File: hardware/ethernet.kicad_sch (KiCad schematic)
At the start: 31 parts, among them J2 HR871150C, U2 W5500, X2 25MHz

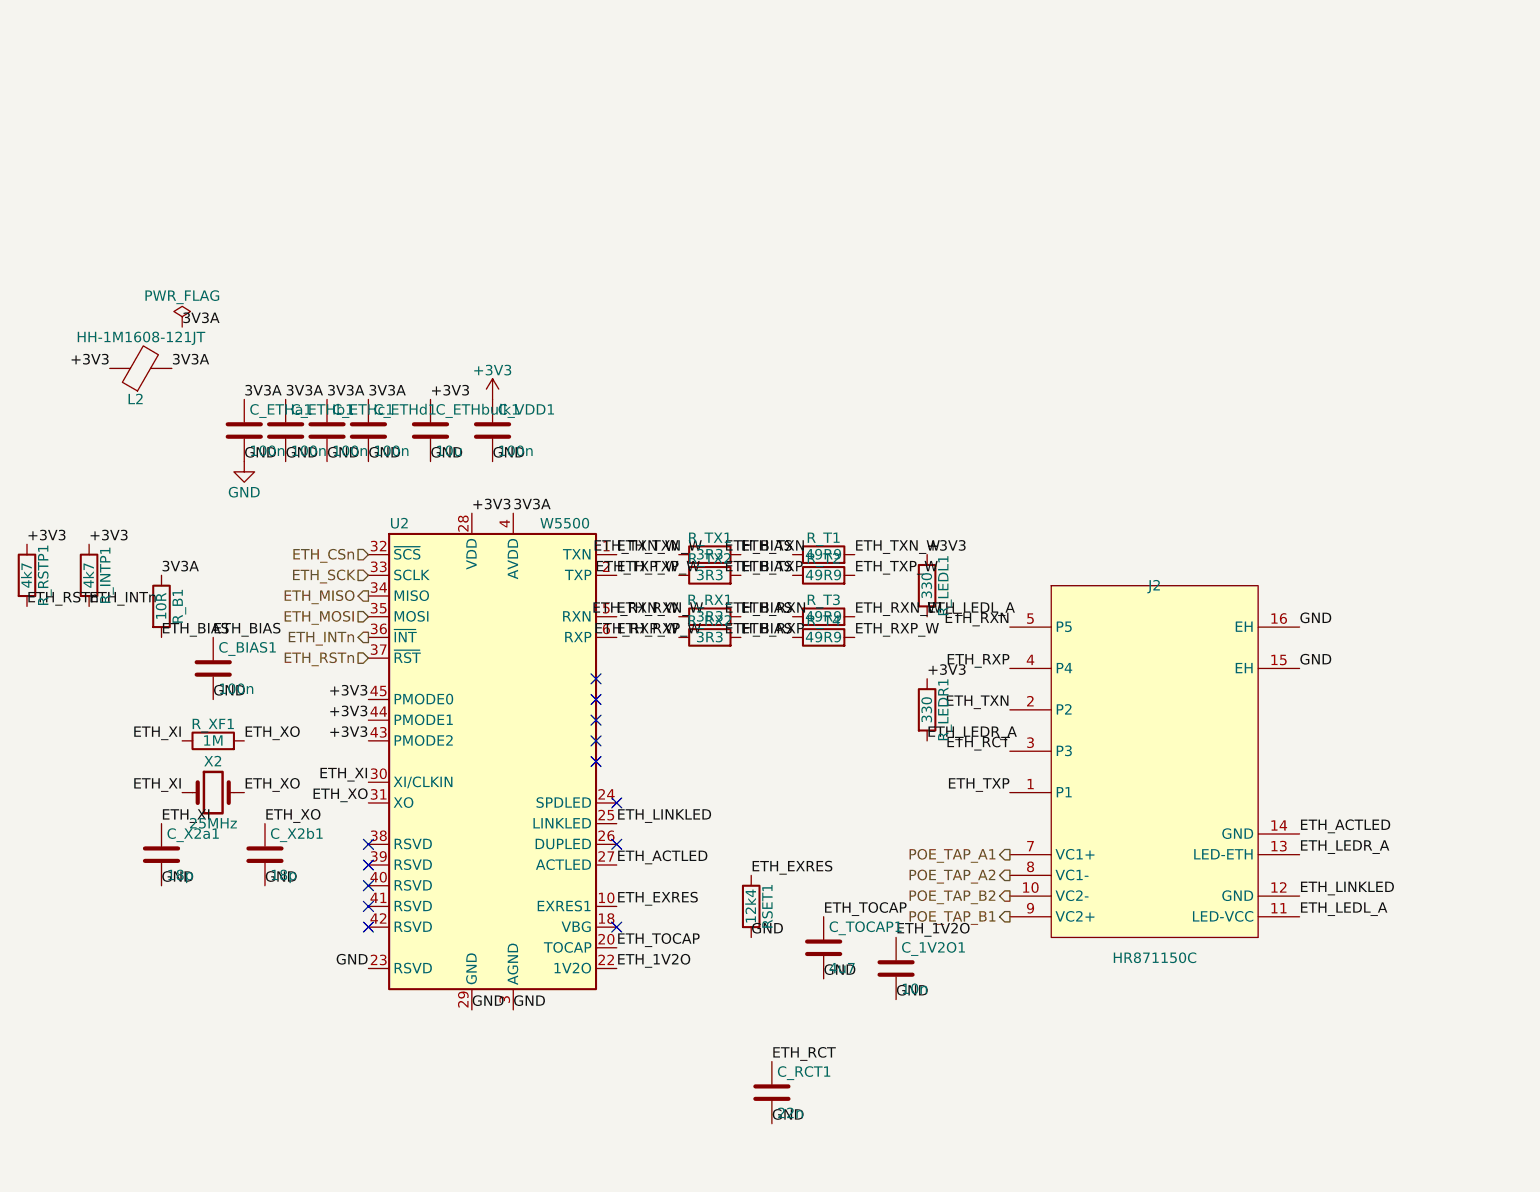
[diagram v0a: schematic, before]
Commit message: hardware: updated board design (reference renumbering, LED polarity fix, crystal symbol upgrade)
Replaces the schematics/PCB/project file with the latest design. Key
changes, verified before committing (netlist-check.py: 124 checks, 0
failures; ERC unchanged at 3 known pin_not_driven findings on W5500 SPI
inputs, same severity-policy artifact as before):

- Component reference designators changed from descriptive names
  (R_ATN, C_3V3, D_BR1, etc.) to plain auto-numbered ones (R15, C9, D1,
  etc.) -- intentional, since descriptive names were ending up on the
  silkscreen; they belong in the BOM instead. docs/netlist-spec.nets
  updated to match via a UUID-verified old-ref -> new-ref mapping (every
  renamed symbol's KiCad UUID was unchanged, confirming these are pure
  renames with no electrical difference), not a hand transcription.
- LED1's wiring was corrected: the old schematic had its anode tied to
  GND and cathode driven by LED_A (backwards -- confirmed via each net's
  pinfunction annotation in the exported netlist, K_1/A_2, which is
  fixed by the Device:LED symbol regardless of reference numbering).
  The new schematic has cathode-to-GND, anode-to-LED_A, the correct
  orientation.
- X1/X2 changed from Device:Crystal (2-pin) to Device:Crystal_GND24
  (4-pin, case-ground on pins 2/4) -- a more accurate symbol for the
  real SMD crystal package. netlist-spec.nets updated accordingly
  (XOUT/ETH_XO now reference pin 3, GND gained the four case pins).

mcu.kicad_sch was supplied separately (missing from the first archive);
confirmed it has no further sub-sheet references and all its symbols'
footprint names resolve against the existing hardware/lib/adapter.pretty/
library, which was deliberately left untouched along with fp-lib-table,
sym-lib-table, and .konnect/ -- none of those changed in this update.
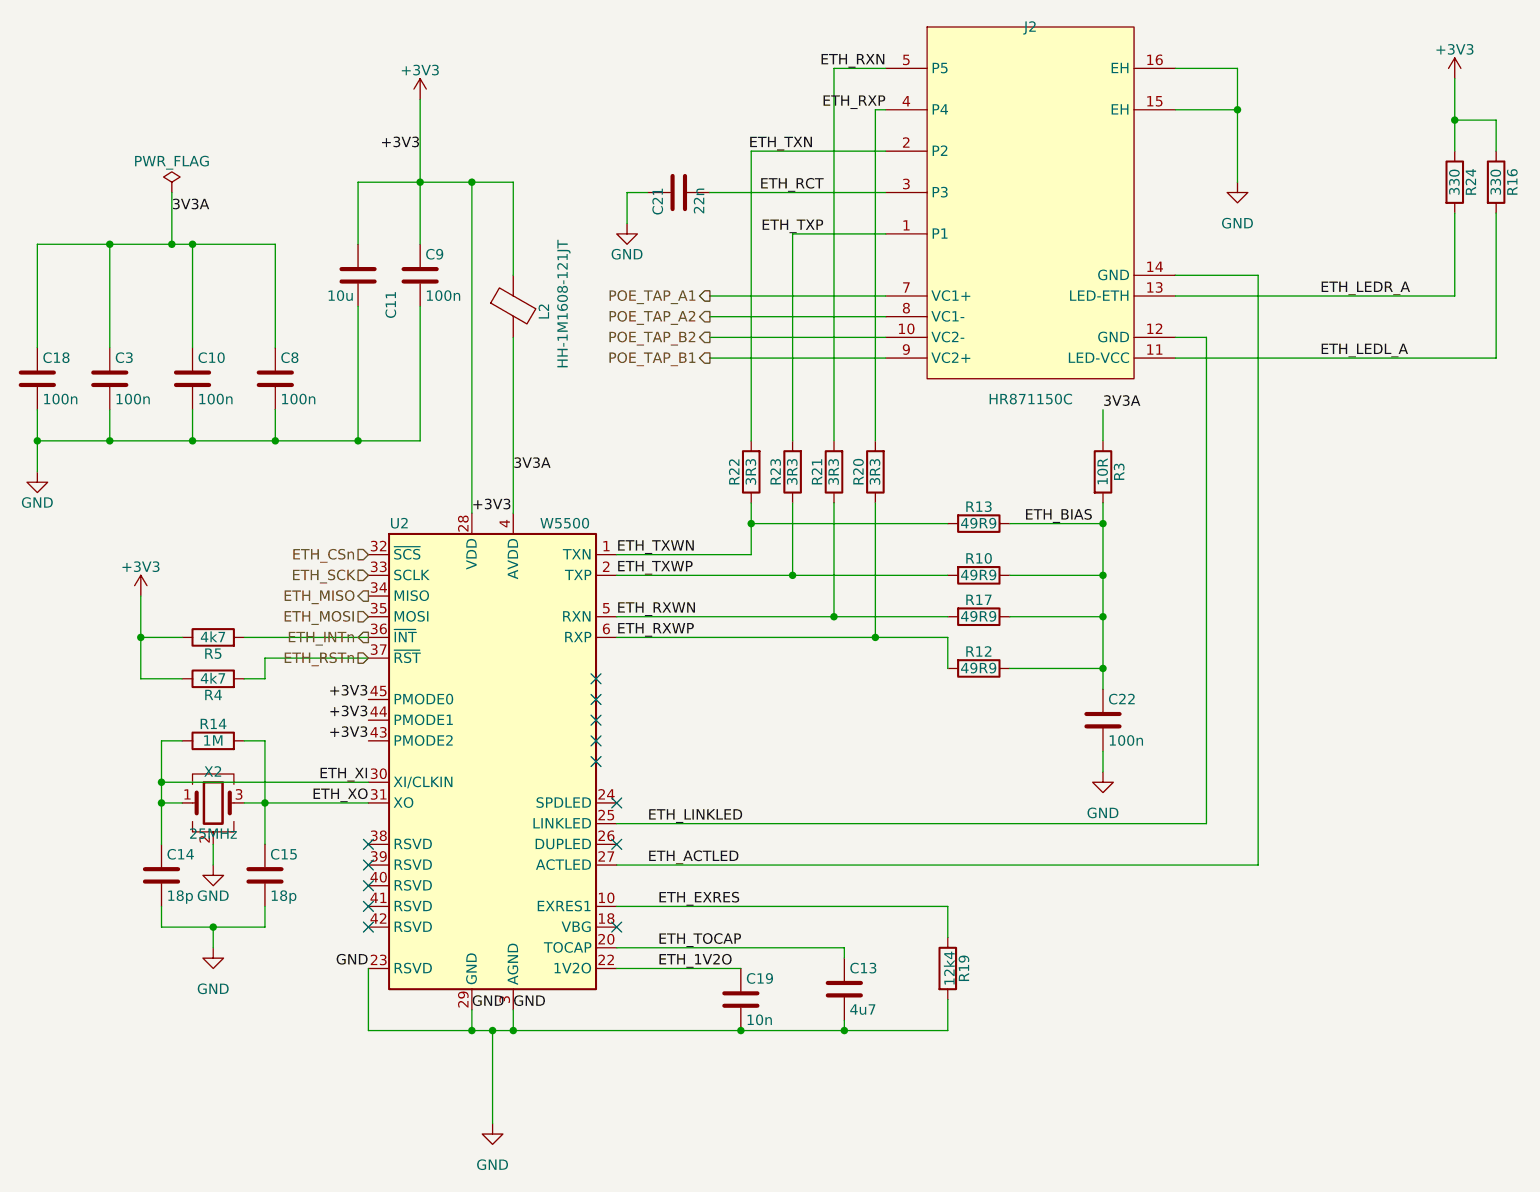
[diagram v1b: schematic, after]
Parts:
- C19: renamed from C_1V2O1; LCSC (none) -> C1710
- J2: LCSC (none) -> C19724786
- U2: LCSC (none) -> C32843
- X2: symbol Device:Crystal -> Device:Crystal_GND24; LCSC Part (none) -> C9006; MPN (none) -> X322525MOB4SI; Manufacturer (none) -> YXC Crystal Oscillators
- renumbered C_ETHc1 to C10, C_ETHbulk1 to C11, C_TOCAP1 to C13, C_X2a1 to C14, C_X2b1 to C15, C_ETHa1 to C18, C_RCT1 to C21, C_BIAS1 to C22, C_ETHb1 to C3, C_ETHd1 to C8, C_VDD1 to C9, R_T2 to R10, R_T4 to R12, R_T1 to R13, R_XF1 to R14, R_LEDL1 to R16, R_T3 to R17, RSET1 to R19, R_RX2 to R20, R_RX1 to R21, R_TX1 to R22, R_TX2 to R23, R_LEDR1 to R24, R_B1 to R3, R_RSTP1 to R4, R_INTP1 to R5
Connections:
- net ETH_XO: now also X2.3; no longer X2.2
- net GND: now also X2.2 (G), X2.4 (G)
- net ETH_RXN_W renamed ETH_RXWN
- net ETH_RXP_W renamed ETH_RXWP
- net ETH_TXN_W renamed ETH_TXWN
- net ETH_TXP_W renamed ETH_TXWP
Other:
- moved on the sheet: C10, C11, C13, C14, C15, C18, C19, C21, C22, C3, C8, C9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
